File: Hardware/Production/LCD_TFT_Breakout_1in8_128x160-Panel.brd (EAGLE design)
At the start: 40.6 x 59.7 mm, 62 parts, among them J1 MICRO-SD_CARD_SOCKETTINY, Q1 220mA/50V/3.5Ω, U2 TXB0108DQSR, U3 3.3V

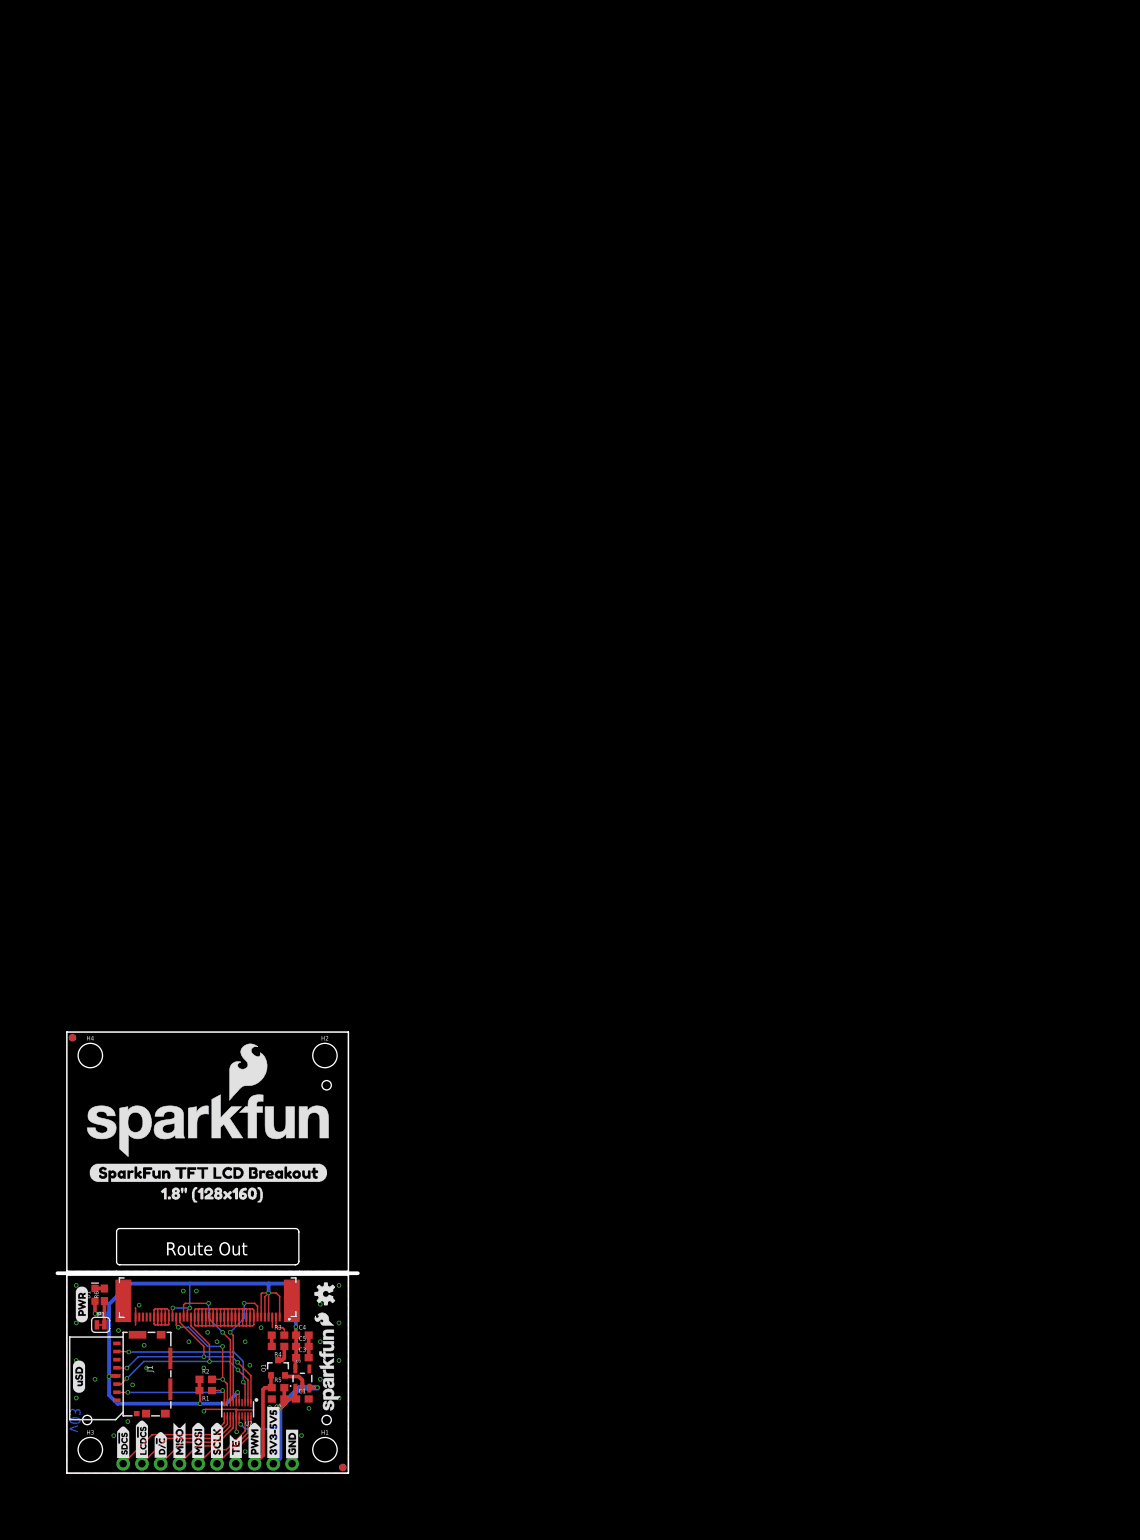
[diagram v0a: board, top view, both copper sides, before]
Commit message: Panelize and CAM prototypes
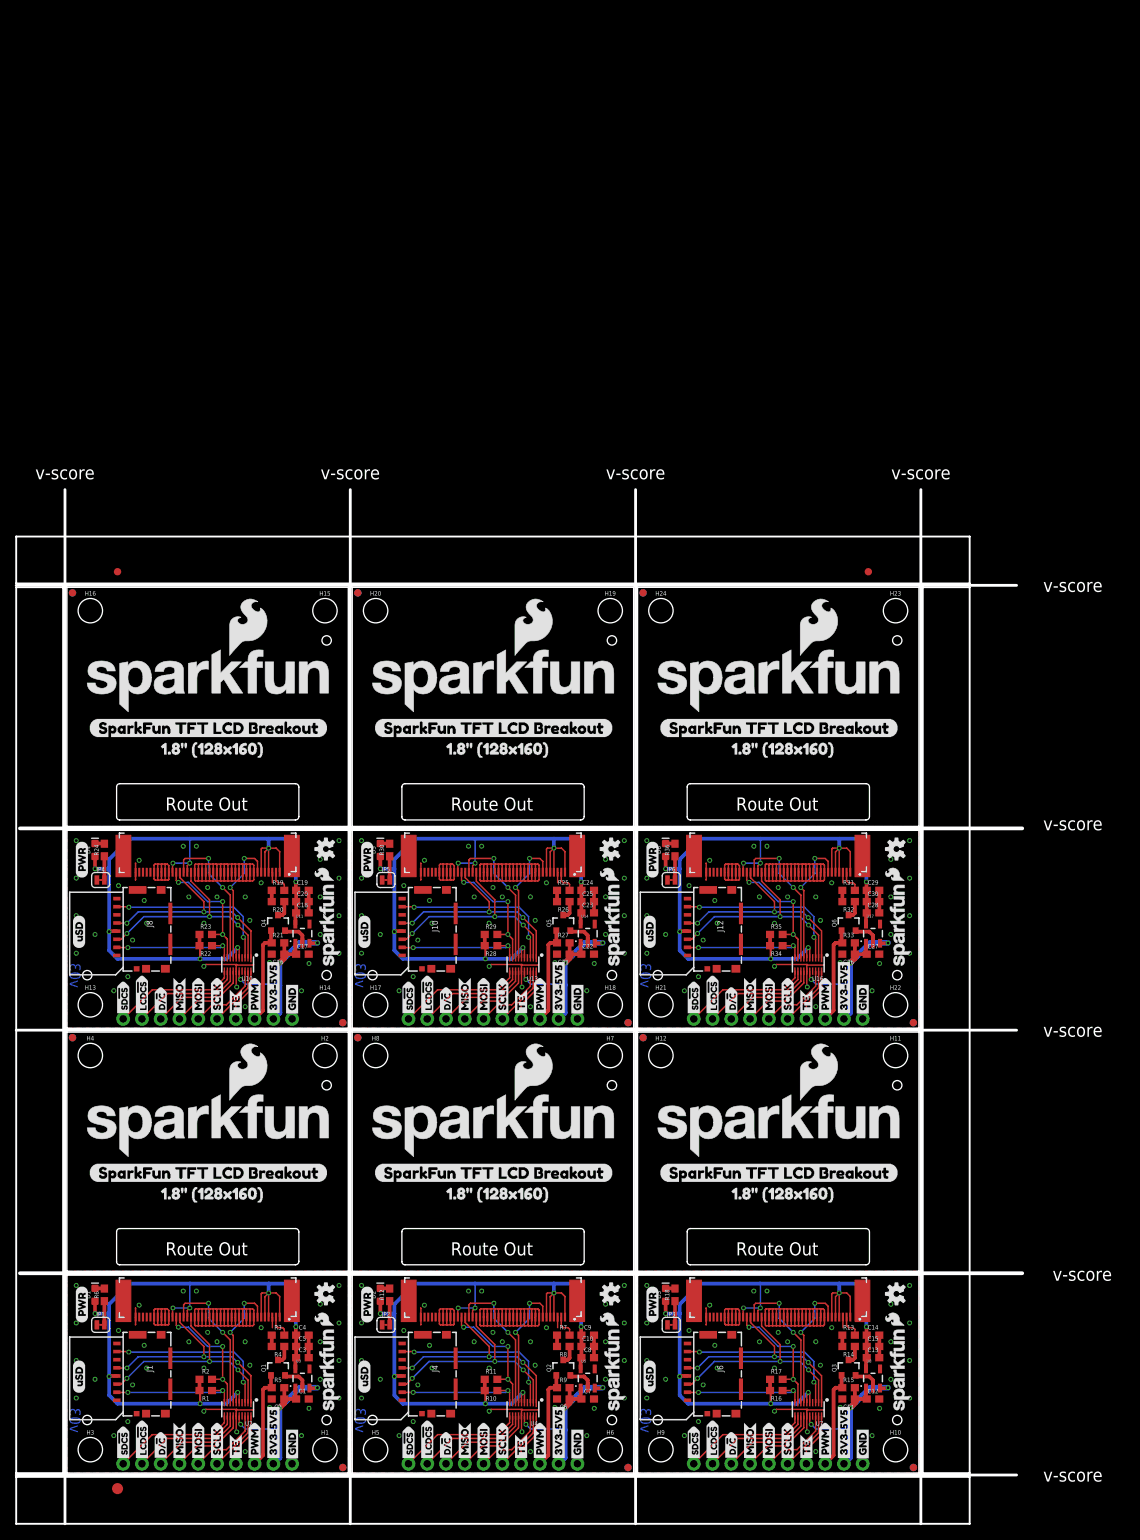
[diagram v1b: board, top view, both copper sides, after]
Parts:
- removed FRAME1: FRAME-LETTER, SparkFun-Aesthetics:CREATIVE_COMMONS
- added C10, C11, C15, C16, C20, C21, C25, C26, C30, C6: 0.1uF, SparkFun-Capacitors:0603
- added C12, C14, C17, C19, C22, C24, C27, C29, C7, C9: 1.0uF, SparkFun-Capacitors:0603
- added C13, C18, C23, C28, C8: 4.7uF, SparkFun-Capacitors:0603
- added D2, D3, D4, D5, D6: RED, SparkFun-LED:LED-0603
- added E$1, E$2: (no value), SparkFun-Aesthetics:FIDUCIAL-1X2
- added E$3: (no value), SparkFun-Retired:FIDUCIAL-1.5X3
- added FD10, FD11, FD12, FD13, FD14, FD15, FD16, FD17, FD18, FD19, FD20, FD21, FD22, FD23, FD24, FD5, FD6, FD7, FD8, FD9: FIDUCIAL1X2, SparkFun-Aesthetics:FIDUCIAL-1X2
- added H10, H11, H12, H13, H14, H15, H16, H17, H18, H19, H20, H21, H22, H23, H24, H5, H6, H7, H8, H9: STAND-OFF, SparkFun-Hardware:STAND-OFF
- added J10, J12, J4, J6, J8: MICRO-SD_CARD_SOCKETTINY, SparkFun-Connectors:MICROSD_TINY
- added J11, J3, J5, J7, J9: (no value), SparkFun-Connectors:1X10_NO_SILK
- added JP2, JP3, JP4, JP5, JP6: LED, SparkFun-Jumpers:SMT-JUMPER_2_NC_TRACE_SILK
- added LOGO10, LOGO12, LOGO4, LOGO6, LOGO8: OSHW-LOGOS, SparkFun-Aesthetics:OSHW-LOGO-S
- added LOGO11, LOGO5, LOGO7, LOGO9: SFE_LOGO_NAME_FLAME.3_INCH, SparkFun-Aesthetics:SFE_LOGO_NAME_FLAME_.3
- added Q2, Q3, Q4, Q5, Q6: 220mA/50V/3.5Ω, SparkFun-DiscreteSemi:SOT23-3
- added R10, R11, R15, R16, R17, R21, R22, R23, R27, R28, R29, R33, R34, R35, R9: 10k, SparkFun-Resistors:0603
- added R12, R18, R24, R30, R36: 1k, SparkFun-Resistors:0603
- added R13, R14, R19, R20, R25, R26, R31, R32, R7, R8: 1, SparkFun-Resistors:0603
- added U$100, U$112, U$131, U$143, U$162, U$174, U$38, U$50, U$69, U$81: (no value), buzzard_labels:MOSI2
- added U$101, U$113, U$132, U$144, U$163, U$175, U$39, U$51, U$70, U$82: (no value), buzzard_labels:SCLK4
- added U$102, U$114, U$133, U$145, U$164, U$176, U$40, U$52, U$71, U$83: (no value), buzzard_labels:TE5
- added U$103, U$115, U$134, U$146, U$165, U$177, U$41, U$53, U$72, U$84: (no value), buzzard_labels:PWM6
- added U$104, U$135, U$166, U$42, U$73: (no value), title:SPARKFUN_TFT_LCD_BREAKOUT1
- added U$105, U$136, U$167, U$43, U$74: (no value), title:1#8#_#128X160#1
- added U$106, U$108, U$137, U$139, U$168, U$170, U$44, U$46, U$75, U$77: (no value), title:SPARKFUN_TFT_LCD_BREAKOUT2
- added U$107, U$109, U$138, U$140, U$169, U$171, U$45, U$47, U$76, U$78: (no value), title:1#8#_#128X160#0
- added U$110, U$127, U$141, U$158, U$172, U$34, U$48, U$65, U$79, U$96: (no value), buzzard_labels:D##C7
- added U$111, U$130, U$142, U$161, U$173, U$37, U$49, U$68, U$80, U$99: (no value), buzzard_labels:MISO3
- added U$116, U$128, U$147, U$159, U$178, U$35, U$54, U$66, U$85, U$97: (no value), buzzard_labels:GND0
- added U$117, U$118, U$148, U$149, U$179, U$180, U$55, U$56, U$86, U$87: (no value), cs:LCD#CS1
- added U$119, U$120, U$150, U$151, U$181, U$182, U$57, U$58, U$88, U$89: (no value), cs:SD#CS0
- added U$121, U$152, U$183, U$59, U$90: (no value), cs:USD2
- added U$122, U$153, U$184, U$60, U$91: (no value), cs:PWR4
- added U$123, U$154, U$185, U$61, U$92: EXTERNAL_DISP-KWH018ST14-F01, SparkFun-Displays:KWH018ST14-F01_HOLES
- added U$124, U$155, U$186, U$62, U$93: (no value), V3to5:3V3#5V50
- added U$125, U$156, U$17, U$63, U$94: (no value), SparkFun-Aesthetics:SFE_LOGO_NAME_.1
- added U$126, U$157, U$31, U$64, U$95: (no value), SparkFun-Aesthetics:SFE_LOGO_FLAME_.1
- added U$129, U$160, U$36, U$67, U$98: (no value), buzzard_labels:VIN1
- added U10, U13, U16, U4, U7: TXB0108DQSR, SparkFun-IC-Comms:UFDFN-20
- added U11, U14, U17, U5, U8: 3.3V, SparkFun-IC-Power:SOT23-5
- added U12, U15, U18, U6, U9: (no value), SparkFun-Displays:FPC05040-17204
- LOGO2: value SPECIAL_INSTRUCTIONS-PRODUCTION -> SFE_LOGO_NAME_FLAME.3_INCH; device SparkFun-Aesthetics:PRODUCTION_INSTRUCTIONS -> SparkFun-Aesthetics:SFE_LOGO_NAME_FLAME_.3
- moved LOGO2 119.9 mm to (57.7, 47.0)
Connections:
- new net !CS!_IN1: J3.9, U4.12
- new net !CS!_IN2: J5.9, U7.12
- new net !CS!_IN3: J7.9, U10.12
- new net !CS!_IN4: J9.9, U13.12
- new net !CS!_IN5: J11.9, U16.12
- new net !CS1: R11.2, U4.9, U6.P$29
- new net !CS2: R17.2, U7.9, U9.P$29
- new net !CS3: R23.2, U10.9, U12.P$29
- new net !CS4: R29.2, U13.9, U15.P$29
- new net !CS5: R35.2, U16.9, U18.P$29
- new net 3.3V1: C10.1, C8.1, C9.1, D2.A, J4.4, R10.2, R11.1, U4.5, U4.6, U5.5, U6.P$1, U6.P$26, U6.P$30, U6.P$4, U6.P$5, U6.P$6
- new net 3.3V2: C13.1, C14.1, C15.1, D3.A, J6.4, R16.2, R17.1, U7.5, U7.6, U8.5, U9.P$1, U9.P$26, U9.P$30, U9.P$4, U9.P$5, U9.P$6
- new net 3.3V3: C18.1, C19.1, C20.1, D4.A, J8.4, R22.2, R23.1, U10.5, U10.6, U11.5, U12.P$1, U12.P$26, U12.P$30, U12.P$4, U12.P$5, U12.P$6
- new net 3.3V4: C23.1, C24.1, C25.1, D5.A, J10.4, R28.2, R29.1, U13.5, U13.6, U14.5, U15.P$1, U15.P$26, U15.P$30, U15.P$4, U15.P$5, U15.P$6
- new net 3.3V5: C28.1, C29.1, C30.1, D6.A, J12.4, R34.2, R35.1, U16.5, U16.6, U17.5, U18.P$1, U18.P$26, U18.P$30, U18.P$4, U18.P$5, U18.P$6
- new net D/!C!_IN1: J3.8, U4.13
- new net D/!C!_IN2: J5.8, U7.13
- new net D/!C!_IN3: J7.8, U10.13
- new net D/!C!_IN4: J9.8, U13.13
- new net D/!C!_IN5: J11.8, U16.13
- new net D/!C1: U4.8, U6.P$27
- new net D/!C2: U7.8, U9.P$27
- new net D/!C3: U10.8, U12.P$27
- new net D/!C4: U13.8, U15.P$27
- new net D/!C5: U16.8, U18.P$27
- new net GND1: C10.2, C6.2, C7.2, C8.2, C9.2, J3.1, J4.6, JP2.1, Q2.2, U4.15, U5.2, U6.P$10, U6.P$11, U6.P$12, U6.P$13, U6.P$14, U6.P$15, U6.P$16, U6.P$17, U6.P$18, U6.P$19, U6.P$20, U6.P$21, U6.P$22, U6.P$23, U6.P$24, U6.P$3, U6.P$31, U6.P$32, U6.P$33, U6.P$34, U6.P$35, U6.P$40, U6.P$8, U6.P$9
- new net GND2: C11.2, C12.2, C13.2, C14.2, C15.2, J5.1, J6.6, JP3.1, Q3.2, U7.15, U8.2, U9.P$10, U9.P$11, U9.P$12, U9.P$13, U9.P$14, U9.P$15, U9.P$16, U9.P$17, U9.P$18, U9.P$19, U9.P$20, U9.P$21, U9.P$22, U9.P$23, U9.P$24, U9.P$3, U9.P$31, U9.P$32, U9.P$33, U9.P$34, U9.P$35, U9.P$40, U9.P$8, U9.P$9
- new net GND3: C16.2, C17.2, C18.2, C19.2, C20.2, J7.1, J8.6, JP4.1, Q4.2, U10.15, U11.2, U12.P$10, U12.P$11, U12.P$12, U12.P$13, U12.P$14, U12.P$15, U12.P$16, U12.P$17, U12.P$18, U12.P$19, U12.P$20, U12.P$21, U12.P$22, U12.P$23, U12.P$24, U12.P$3, U12.P$31, U12.P$32, U12.P$33, U12.P$34, U12.P$35, U12.P$40, U12.P$8, U12.P$9
- new net GND4: C21.2, C22.2, C23.2, C24.2, C25.2, J10.6, J9.1, JP5.1, Q5.2, U13.15, U14.2, U15.P$10, U15.P$11, U15.P$12, U15.P$13, U15.P$14, U15.P$15, U15.P$16, U15.P$17, U15.P$18, U15.P$19, U15.P$20, U15.P$21, U15.P$22, U15.P$23, U15.P$24, U15.P$3, U15.P$31, U15.P$32, U15.P$33, U15.P$34, U15.P$35, U15.P$40, U15.P$8, U15.P$9
- new net GND5: C26.2, C27.2, C28.2, C29.2, C30.2, J11.1, J12.6, JP6.1, Q6.2, U16.15, U17.2, U18.P$10, U18.P$11, U18.P$12, U18.P$13, U18.P$14, U18.P$15, U18.P$16, U18.P$17, U18.P$18, U18.P$19, U18.P$20, U18.P$21, U18.P$22, U18.P$23, U18.P$24, U18.P$3, U18.P$31, U18.P$32, U18.P$33, U18.P$34, U18.P$35, U18.P$40, U18.P$8, U18.P$9
- new net LEDK1: R7.2, U6.P$2
- new net LEDK2: R13.2, U9.P$2
- new net LEDK3: R19.2, U12.P$2
- new net LEDK4: R25.2, U15.P$2
- new net LEDK5: R31.2, U18.P$2
- new net LED_PWM1: J3.3, Q2.1, R9.1
- new net LED_PWM2: J5.3, Q3.1, R15.1
- new net LED_PWM3: J7.3, Q4.1, R21.1
- new net LED_PWM4: J9.3, Q5.1, R27.1
- new net LED_PWM5: J11.3, Q6.1, R33.1
- new net MISO1: J4.7, U4.3
- new net MISO2: J6.7, U7.3
- new net MISO3: J8.7, U10.3
- new net MISO4: J10.7, U13.3
- new net MISO5: J12.7, U16.3
- new net MISO_IN1: J3.6, U4.18
- new net MISO_IN2: J5.6, U7.18
- new net MISO_IN3: J7.6, U10.18
- new net MISO_IN4: J9.6, U13.18
- new net MISO_IN5: J11.6, U16.18
- new net MOSI1: J4.3, U4.2, U6.P$25
- new net MOSI2: J6.3, U7.2, U9.P$25
- new net MOSI3: J8.3, U10.2, U12.P$25
- new net MOSI4: J10.3, U13.2, U15.P$25
- new net MOSI5: J12.3, U16.2, U18.P$25
- new net MOSI_IN1: J3.5, U4.19
- new net MOSI_IN2: J5.5, U7.19
- new net MOSI_IN3: J7.5, U10.19
- new net MOSI_IN4: J9.5, U13.19
- new net MOSI_IN5: J11.5, U16.19
- new net N$10: R7.1, R8.2
- new net N$14: Q3.3, R14.1
- new net N$16: D3.C, R18.2
- new net N$17: JP3.2, R18.1
- new net N$18: R13.1, R14.2
- new net N$21: Q4.3, R20.1
- new net N$23: D4.C, R24.2
- new net N$24: JP4.2, R24.1
- new net N$25: R19.1, R20.2
- new net N$29: Q5.3, R26.1
- new net N$31: D5.C, R30.2
- new net N$32: JP5.2, R30.1
- new net N$33: R25.1, R26.2
- new net N$36: Q6.3, R32.1
- new net N$38: D6.C, R36.2
- new net N$39: JP6.2, R36.1
- new net N$4: Q2.3, R8.1
- new net N$40: R31.1, R32.2
- new net N$7: D2.C, R12.2
- new net N$9: JP2.2, R12.1
- new net SCLK1: J4.5, U4.1, U6.P$28
- new net SCLK2: J6.5, U7.1, U9.P$28
- new net SCLK3: J8.5, U10.1, U12.P$28
- new net SCLK4: J10.5, U13.1, U15.P$28
- new net SCLK5: J12.5, U16.1, U18.P$28
- new net SCLK_IN1: J3.4, U4.20
- new net SCLK_IN2: J5.4, U7.20
- new net SCLK_IN3: J7.4, U10.20
- new net SCLK_IN4: J9.4, U13.20
- new net SCLK_IN5: J11.4, U16.20
- new net SD_!CS!_IN1: J3.10, U4.11
- new net SD_!CS!_IN2: J5.10, U7.11
- new net SD_!CS!_IN3: J7.10, U10.11
- new net SD_!CS!_IN4: J9.10, U13.11
- new net SD_!CS!_IN5: J11.10, U16.11
- new net SD_!CS1: J4.2, R10.1, U4.10
- new net SD_!CS2: J6.2, R16.1, U7.10
- new net SD_!CS3: J8.2, R22.1, U10.10
- new net SD_!CS4: J10.2, R28.1, U13.10
- new net SD_!CS5: J12.2, R34.1, U16.10
- new net TE1: U4.7, U6.P$7
- new net TE2: U7.7, U9.P$7
- new net TE3: U10.7, U12.P$7
- new net TE4: U13.7, U15.P$7
- new net TE5: U16.7, U18.P$7
- new net TE_IN1: J3.7, U4.14
- new net TE_IN2: J5.7, U7.14
- new net TE_IN3: J7.7, U10.14
- new net TE_IN4: J9.7, U13.14
- new net TE_IN5: J11.7, U16.14
- new net VIN1: C6.1, C7.1, J3.2, R9.2, U4.16, U5.1, U5.3
- new net VIN2: C11.1, C12.1, J5.2, R15.2, U7.16, U8.1, U8.3
- new net VIN3: C16.1, C17.1, J7.2, R21.2, U10.16, U11.1, U11.3
- new net VIN4: C21.1, C22.1, J9.2, R27.2, U13.16, U14.1, U14.3
- new net VIN5: C26.1, C27.1, J11.2, R33.2, U16.16, U17.1, U17.3
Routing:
- net 3.3V3: track 0.00 -> 104.1 mm, vias 0 -> 8
- net 3.3V4: track 0.00 -> 104.1 mm, vias 0 -> 8
- net 3.3V1: track 0.00 -> 104.1 mm, vias 0 -> 8
- net 3.3V5: track 0.00 -> 104.1 mm, vias 0 -> 8
- net 3.3V2: track 0.00 -> 104.1 mm, vias 0 -> 8
- net GND5: track 0.00 -> 90.1 mm, vias 0 -> 31
- net GND4: track 0.00 -> 90.1 mm, vias 0 -> 31
- net GND3: track 0.00 -> 90.1 mm, vias 0 -> 31
- net GND2: track 0.00 -> 90.1 mm, vias 0 -> 31
- net GND1: track 0.00 -> 90.1 mm, vias 0 -> 31
- net SCLK3: track 0.00 -> 30.3 mm, vias 0 -> 3
- net SCLK4: track 0.00 -> 30.3 mm, vias 0 -> 3
- net SCLK1: track 0.00 -> 30.3 mm, vias 0 -> 3
- net SCLK5: track 0.00 -> 30.3 mm, vias 0 -> 3
- net SCLK2: track 0.00 -> 30.3 mm, vias 0 -> 3
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- added copper zone on layer 1, net GND1
- added copper zone on layer 16, net GND1
- added copper zone on layer 1, net GND2
- added copper zone on layer 16, net GND2
- added copper zone on layer 1, net GND3
- added copper zone on layer 16, net GND3
- added copper zone on layer 1, net GND4
- added copper zone on layer 16, net GND4
- added copper zone on layer 1, net GND5
- added copper zone on layer 16, net GND5
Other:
- board size 40.6 x 59.7 mm -> 136.1 x 140 mm
- board text added: "v-score"
- board text removed: "IN"
- board text removed: "Owen Lyke"
- board text removed: "When panelizing please extend the mid-board v-score lines across the panel without changing location. This is a break-away option for the user"

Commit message: panel
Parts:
- added FD25, FD26, FD27, FD28, FD29, FD30, FD31, FD32, FD33, FD34, FD35, FD36: FIDUCIAL1X2, SparkFun-Aesthetics:FIDUCIAL-1X2
- added FRAME1, FRAME2, FRAME3, FRAME4, FRAME5, FRAME6: FRAME-LETTER, SparkFun-Aesthetics:CREATIVE_COMMONS
- added LOGO13, LOGO16: SPECIAL_INSTRUCTIONS-PRODUCTION, SparkFun-Aesthetics:PRODUCTION_INSTRUCTIONS
- added LOGO14, LOGO17: SFE_LOGO_NAME_FLAME.3_INCH, SparkFun-Aesthetics:SFE_LOGO_NAME_FLAME_.3
- added LOGO15, LOGO18: OSHW-LOGOS, SparkFun-Aesthetics:OSHW-LOGO-S
- added U$187: (no value), buzzard_labels:PWM6
- added U$188: (no value), buzzard_labels:GND0
- added U$189, U$190: (no value), cs:LCD#CS1
- added U$191, U$192: (no value), cs:SD#CS0
- added U$193: (no value), cs:USD2
- added U$194: (no value), cs:PWR4
- added U$195: EXTERNAL_DISP-KWH018ST14-F01, SparkFun-Displays:KWH018ST14-F01_HOLES
- added U$196: (no value), V3to5:3V3#5V50
- added U$197: (no value), buzzard_labels:10
- added U$198: (no value), buzzard_labels:401
- LOGO10, LOGO4: value OSHW-LOGOS -> SPECIAL_INSTRUCTIONS-PRODUCTION; device SparkFun-Aesthetics:OSHW-LOGO-S -> SparkFun-Aesthetics:PRODUCTION_INSTRUCTIONS
- LOGO2, LOGO7: value SFE_LOGO_NAME_FLAME.3_INCH -> SPECIAL_INSTRUCTIONS-PRODUCTION; device SparkFun-Aesthetics:SFE_LOGO_NAME_FLAME_.3 -> SparkFun-Aesthetics:PRODUCTION_INSTRUCTIONS
- LOGO8: value OSHW-LOGOS -> SFE_LOGO_NAME_FLAME.3_INCH; device SparkFun-Aesthetics:OSHW-LOGO-S -> SparkFun-Aesthetics:SFE_LOGO_NAME_FLAME_.3
- LOGO9: value SFE_LOGO_NAME_FLAME.3_INCH -> OSHW-LOGOS; device SparkFun-Aesthetics:SFE_LOGO_NAME_FLAME_.3 -> SparkFun-Aesthetics:OSHW-LOGO-S
- U$100: device buzzard_labels:MOSI2 -> SparkFun-Aesthetics:SFE_LOGO_NAME_.1
- U$101: device buzzard_labels:SCLK4 -> SparkFun-Aesthetics:SFE_LOGO_FLAME_.1
- U$102, U$83: device buzzard_labels:TE5 -> buzzard_labels:D##C7
- U$103: device buzzard_labels:PWM6 -> buzzard_labels:GND0
- U$104: device title:SPARKFUN_TFT_LCD_BREAKOUT1 -> buzzard_labels:VIN1
- U$105: device title:1#8#_#128X160#1 -> buzzard_labels:MISO3
- U$106, U$139: device title:SPARKFUN_TFT_LCD_BREAKOUT2 -> buzzard_labels:MOSI2
- U$107, U$140: device title:1#8#_#128X160#0 -> buzzard_labels:SCLK4
- U$108, U$75: device title:SPARKFUN_TFT_LCD_BREAKOUT2 -> buzzard_labels:TE5
- U$109, U$76: device title:1#8#_#128X160#0 -> buzzard_labels:PWM6
- U$110: device buzzard_labels:D##C7 -> title:SPARKFUN_TFT_LCD_BREAKOUT1
- U$111: device buzzard_labels:MISO3 -> title:1#8#_#128X160#1
- U$112, U$81: device buzzard_labels:MOSI2 -> title:SPARKFUN_TFT_LCD_BREAKOUT2
- U$113, U$82: device buzzard_labels:SCLK4 -> title:1#8#_#128X160#0
- U$114, U$145: device buzzard_labels:TE5 -> title:SPARKFUN_TFT_LCD_BREAKOUT2
- U$115, U$146: device buzzard_labels:PWM6 -> title:1#8#_#128X160#0
- U$116: device buzzard_labels:GND0 -> buzzard_labels:D##C7
- U$117: device cs:LCD#CS1 -> buzzard_labels:MISO3
- U$118: device cs:LCD#CS1 -> buzzard_labels:MOSI2
- U$119: device cs:SD#CS0 -> buzzard_labels:SCLK4
- U$120: device cs:SD#CS0 -> buzzard_labels:TE5
- U$121: device cs:USD2 -> buzzard_labels:PWM6
- U$122: device cs:PWR4 -> buzzard_labels:GND0
- U$123: value EXTERNAL_DISP-KWH018ST14-F01 -> (none); device SparkFun-Displays:KWH018ST14-F01_HOLES -> cs:LCD#CS1
- U$124: device V3to5:3V3#5V50 -> cs:LCD#CS1
- U$125: device SparkFun-Aesthetics:SFE_LOGO_NAME_.1 -> cs:SD#CS0
- U$126: device SparkFun-Aesthetics:SFE_LOGO_FLAME_.1 -> cs:SD#CS0
- U$127: device buzzard_labels:D##C7 -> cs:USD2
- U$128: device buzzard_labels:GND0 -> cs:PWR4
- U$129: value (none) -> EXTERNAL_DISP-KWH018ST14-F01; device buzzard_labels:VIN1 -> SparkFun-Displays:KWH018ST14-F01_HOLES
- U$130: device buzzard_labels:MISO3 -> V3to5:3V3#5V50
- U$131: device buzzard_labels:MOSI2 -> buzzard_labels:10
- U$132: device buzzard_labels:SCLK4 -> buzzard_labels:401
- U$133: device buzzard_labels:TE5 -> SparkFun-Aesthetics:SFE_LOGO_NAME_.1
- U$134: device buzzard_labels:PWM6 -> SparkFun-Aesthetics:SFE_LOGO_FLAME_.1
- U$135: device title:SPARKFUN_TFT_LCD_BREAKOUT1 -> buzzard_labels:D##C7
- U$136: device title:1#8#_#128X160#1 -> buzzard_labels:GND0
- U$137, U$170: device title:SPARKFUN_TFT_LCD_BREAKOUT2 -> buzzard_labels:VIN1
- U$138, U$171: device title:1#8#_#128X160#0 -> buzzard_labels:MISO3
- U$141: device buzzard_labels:D##C7 -> buzzard_labels:TE5
- U$142: device buzzard_labels:MISO3 -> buzzard_labels:PWM6
- U$143: device buzzard_labels:MOSI2 -> title:SPARKFUN_TFT_LCD_BREAKOUT1
- U$144: device buzzard_labels:SCLK4 -> title:1#8#_#128X160#1
- U$147, U$178: device buzzard_labels:GND0 -> title:SPARKFUN_TFT_LCD_BREAKOUT2
- U$148, U$179: device cs:LCD#CS1 -> title:1#8#_#128X160#0
- U$149: device cs:LCD#CS1 -> buzzard_labels:D##C7
- U$150: device cs:SD#CS0 -> buzzard_labels:MISO3
- U$151: device cs:SD#CS0 -> buzzard_labels:MOSI2
- U$152: device cs:USD2 -> buzzard_labels:SCLK4
- U$153: device cs:PWR4 -> buzzard_labels:TE5
- U$154: value EXTERNAL_DISP-KWH018ST14-F01 -> (none); device SparkFun-Displays:KWH018ST14-F01_HOLES -> buzzard_labels:PWM6
- U$155: device V3to5:3V3#5V50 -> buzzard_labels:GND0
- U$156: device SparkFun-Aesthetics:SFE_LOGO_NAME_.1 -> cs:LCD#CS1
- U$157: device SparkFun-Aesthetics:SFE_LOGO_FLAME_.1 -> cs:LCD#CS1
- U$158: device buzzard_labels:D##C7 -> cs:SD#CS0
- U$159: device buzzard_labels:GND0 -> cs:SD#CS0
- U$160: device buzzard_labels:VIN1 -> cs:USD2
- U$161: device buzzard_labels:MISO3 -> cs:PWR4
- U$162: value (none) -> EXTERNAL_DISP-KWH018ST14-F01; device buzzard_labels:MOSI2 -> SparkFun-Displays:KWH018ST14-F01_HOLES
- U$163: device buzzard_labels:SCLK4 -> V3to5:3V3#5V50
- U$164: device buzzard_labels:TE5 -> buzzard_labels:10
- U$165: device buzzard_labels:PWM6 -> buzzard_labels:401
- U$166: device title:SPARKFUN_TFT_LCD_BREAKOUT1 -> SparkFun-Aesthetics:SFE_LOGO_NAME_.1
- U$167: device title:1#8#_#128X160#1 -> SparkFun-Aesthetics:SFE_LOGO_FLAME_.1
- U$168: device title:SPARKFUN_TFT_LCD_BREAKOUT2 -> buzzard_labels:D##C7
- U$169: device title:1#8#_#128X160#0 -> buzzard_labels:GND0
- U$17: device SparkFun-Aesthetics:SFE_LOGO_NAME_.1 -> buzzard_labels:10
- U$172: device buzzard_labels:D##C7 -> buzzard_labels:MOSI2
- U$173: device buzzard_labels:MISO3 -> buzzard_labels:SCLK4
- U$174: device buzzard_labels:MOSI2 -> buzzard_labels:TE5
- U$175: device buzzard_labels:SCLK4 -> buzzard_labels:PWM6
- U$176: device buzzard_labels:TE5 -> title:SPARKFUN_TFT_LCD_BREAKOUT1
- U$177: device buzzard_labels:PWM6 -> title:1#8#_#128X160#1
- U$180: device cs:LCD#CS1 -> title:SPARKFUN_TFT_LCD_BREAKOUT2
- U$181: device cs:SD#CS0 -> title:1#8#_#128X160#0
- U$182: device cs:SD#CS0 -> buzzard_labels:D##C7
- U$183: device cs:USD2 -> buzzard_labels:MISO3
- U$184: device cs:PWR4 -> buzzard_labels:MOSI2
- U$185: value EXTERNAL_DISP-KWH018ST14-F01 -> (none); device SparkFun-Displays:KWH018ST14-F01_HOLES -> buzzard_labels:SCLK4
- U$186: device V3to5:3V3#5V50 -> buzzard_labels:TE5
- U$31: device SparkFun-Aesthetics:SFE_LOGO_FLAME_.1 -> buzzard_labels:401
- U$34: device buzzard_labels:D##C7 -> SparkFun-Aesthetics:SFE_LOGO_NAME_.1
- U$35: device buzzard_labels:GND0 -> SparkFun-Aesthetics:SFE_LOGO_FLAME_.1
- U$36: device buzzard_labels:VIN1 -> buzzard_labels:D##C7
- U$37: device buzzard_labels:MISO3 -> buzzard_labels:GND0
- U$38: device buzzard_labels:MOSI2 -> buzzard_labels:VIN1
- U$39, U$51: device buzzard_labels:SCLK4 -> buzzard_labels:MISO3
- U$40, U$52: device buzzard_labels:TE5 -> buzzard_labels:MOSI2
- U$41, U$53: device buzzard_labels:PWM6 -> buzzard_labels:SCLK4
- U$42: device title:SPARKFUN_TFT_LCD_BREAKOUT1 -> buzzard_labels:TE5
- U$43: device title:1#8#_#128X160#1 -> buzzard_labels:PWM6
- U$44, U$77: device title:SPARKFUN_TFT_LCD_BREAKOUT2 -> title:SPARKFUN_TFT_LCD_BREAKOUT1
- U$45, U$78: device title:1#8#_#128X160#0 -> title:1#8#_#128X160#1
- U$48, U$79: device buzzard_labels:D##C7 -> title:SPARKFUN_TFT_LCD_BREAKOUT2
- U$49, U$80: device buzzard_labels:MISO3 -> title:1#8#_#128X160#0
- U$50, U$69: device buzzard_labels:MOSI2 -> buzzard_labels:D##C7
- U$54: device buzzard_labels:GND0 -> buzzard_labels:TE5
- U$55: device cs:LCD#CS1 -> buzzard_labels:PWM6
- U$56: device cs:LCD#CS1 -> buzzard_labels:GND0
- U$57, U$58: device cs:SD#CS0 -> cs:LCD#CS1
- U$59: device cs:USD2 -> cs:SD#CS0
- U$60: device cs:PWR4 -> cs:SD#CS0
- U$61: value EXTERNAL_DISP-KWH018ST14-F01 -> (none); device SparkFun-Displays:KWH018ST14-F01_HOLES -> cs:USD2
- U$62: device V3to5:3V3#5V50 -> cs:PWR4
- U$63: value (none) -> EXTERNAL_DISP-KWH018ST14-F01; device SparkFun-Aesthetics:SFE_LOGO_NAME_.1 -> SparkFun-Displays:KWH018ST14-F01_HOLES
- U$64: device SparkFun-Aesthetics:SFE_LOGO_FLAME_.1 -> V3to5:3V3#5V50
- U$65: device buzzard_labels:D##C7 -> buzzard_labels:10
- U$66: device buzzard_labels:GND0 -> buzzard_labels:401
- U$67: device buzzard_labels:VIN1 -> SparkFun-Aesthetics:SFE_LOGO_NAME_.1
- U$68: device buzzard_labels:MISO3 -> SparkFun-Aesthetics:SFE_LOGO_FLAME_.1
- U$70: device buzzard_labels:SCLK4 -> buzzard_labels:GND0
- U$71: device buzzard_labels:TE5 -> buzzard_labels:VIN1
- U$72, U$84: device buzzard_labels:PWM6 -> buzzard_labels:MISO3
- U$73: device title:SPARKFUN_TFT_LCD_BREAKOUT1 -> buzzard_labels:MOSI2
- U$74: device title:1#8#_#128X160#1 -> buzzard_labels:SCLK4
- U$85: device buzzard_labels:GND0 -> buzzard_labels:MOSI2
- U$86: device cs:LCD#CS1 -> buzzard_labels:SCLK4
- U$87: device cs:LCD#CS1 -> buzzard_labels:TE5
- U$88: device cs:SD#CS0 -> buzzard_labels:PWM6
- U$89: device cs:SD#CS0 -> buzzard_labels:GND0
- U$90: device cs:USD2 -> cs:LCD#CS1
- U$91: device cs:PWR4 -> cs:LCD#CS1
- U$92: value EXTERNAL_DISP-KWH018ST14-F01 -> (none); device SparkFun-Displays:KWH018ST14-F01_HOLES -> cs:SD#CS0
- U$93: device V3to5:3V3#5V50 -> cs:SD#CS0
- U$94: device SparkFun-Aesthetics:SFE_LOGO_NAME_.1 -> cs:USD2
- U$95: device SparkFun-Aesthetics:SFE_LOGO_FLAME_.1 -> cs:PWR4
- U$96: value (none) -> EXTERNAL_DISP-KWH018ST14-F01; device buzzard_labels:D##C7 -> SparkFun-Displays:KWH018ST14-F01_HOLES
- U$97: device buzzard_labels:GND0 -> V3to5:3V3#5V50
- U$98: device buzzard_labels:VIN1 -> buzzard_labels:10
- U$99: device buzzard_labels:MISO3 -> buzzard_labels:401
- moved U$162 145.6 mm to (1.91, 173.7), turned to 0 degrees
- moved U$80 131.0 mm to (27.2, 115.1), flipped to the bottom, turned to 0 degrees
- moved U$77 130.2 mm to (2.92, 100.8), flipped to the top
- moved U$79 129.6 mm to (32.5, 117.6), flipped to the bottom, turned to 0 degrees
- moved U$160 124.1 mm to (1.65, 130.2), flipped to the top
- moved U$165 123.7 mm to (6.35, 139.4), flipped to the top, turned to 0 degrees
- moved U$178 121.7 mm to (71.1, 177.8), flipped to the bottom, turned to 0 degrees
- moved LOGO2 119.9 mm to (-24.5, -40.4)
- moved U$145 119.6 mm to (32.5, 177.8), flipped to the bottom, turned to 0 degrees
- moved U$146 119.4 mm to (27.2, 175.3), flipped to the bottom, turned to 0 degrees
- moved U$161 119.2 mm to (2.03, 139.4), flipped to the top
- moved U$78 118.8 mm to (11.4, 98.0), flipped to the top
- moved U$159 116.7 mm to (7.62, 121.8)
- moved U$179 115.7 mm to (65.8, 175.3), flipped to the bottom, turned to 0 degrees
- moved U$176 115.3 mm to (41.5, 161.0), turned to 0 degrees
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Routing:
- net GND3: track 90.1 -> 94.7 mm, vias 31 -> 39
- net GND5: track 90.1 -> 94.7 mm, vias 31 -> 39
- net GND4: track 90.1 -> 94.7 mm, vias 31 -> 39
- net GND2: track 90.1 -> 94.7 mm, vias 31 -> 39
- net GND: track 90.1 -> 94.7 mm, vias 31 -> 39
- net GND1: track 90.1 -> 94.7 mm, vias 31 -> 39
- net 3.3V2: track 104.1 -> 106.4 mm
- net 3.3V: track 104.1 -> 106.4 mm
- net 3.3V1: track 104.1 -> 106.4 mm
- net 3.3V3: track 104.1 -> 106.4 mm
- net 3.3V5: track 104.1 -> 106.4 mm
- net 3.3V4: track 104.1 -> 106.4 mm
- net SD_!CS4: track 17.6 -> 19.3 mm
- net SD_!CS5: track 17.6 -> 19.3 mm
- net SD_!CS1: track 17.6 -> 19.3 mm
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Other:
- board size 136.1 x 140 mm -> 96.8 x 200.2 mm
- board text added: "IN"
- board text added: "Owen Lyke"
- board text added: "v10"
- board text removed: "v03"
